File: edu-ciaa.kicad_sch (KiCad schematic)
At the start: 2 parts

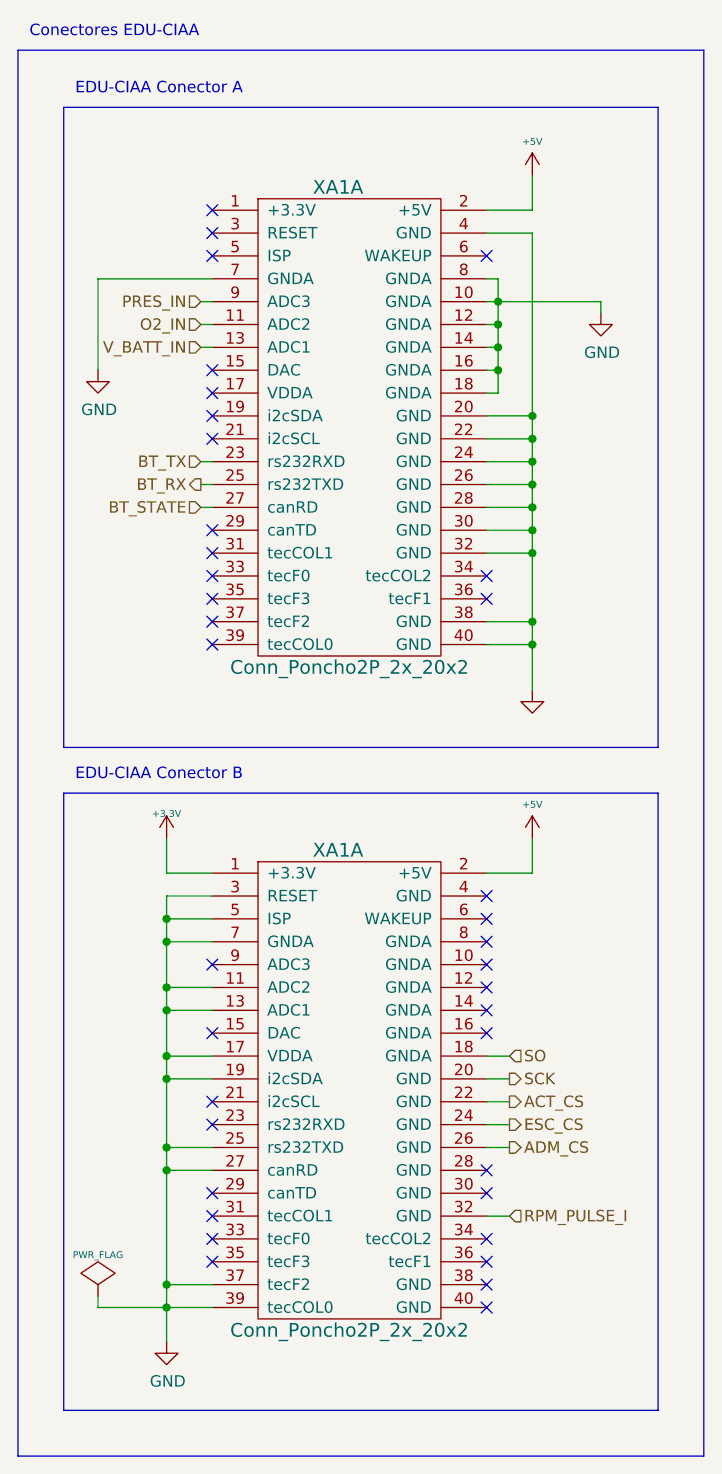
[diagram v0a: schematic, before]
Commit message: Actualizacion a kicad 7, seleccion de ganancia de la etapa de amplificacion de presion de aceite.
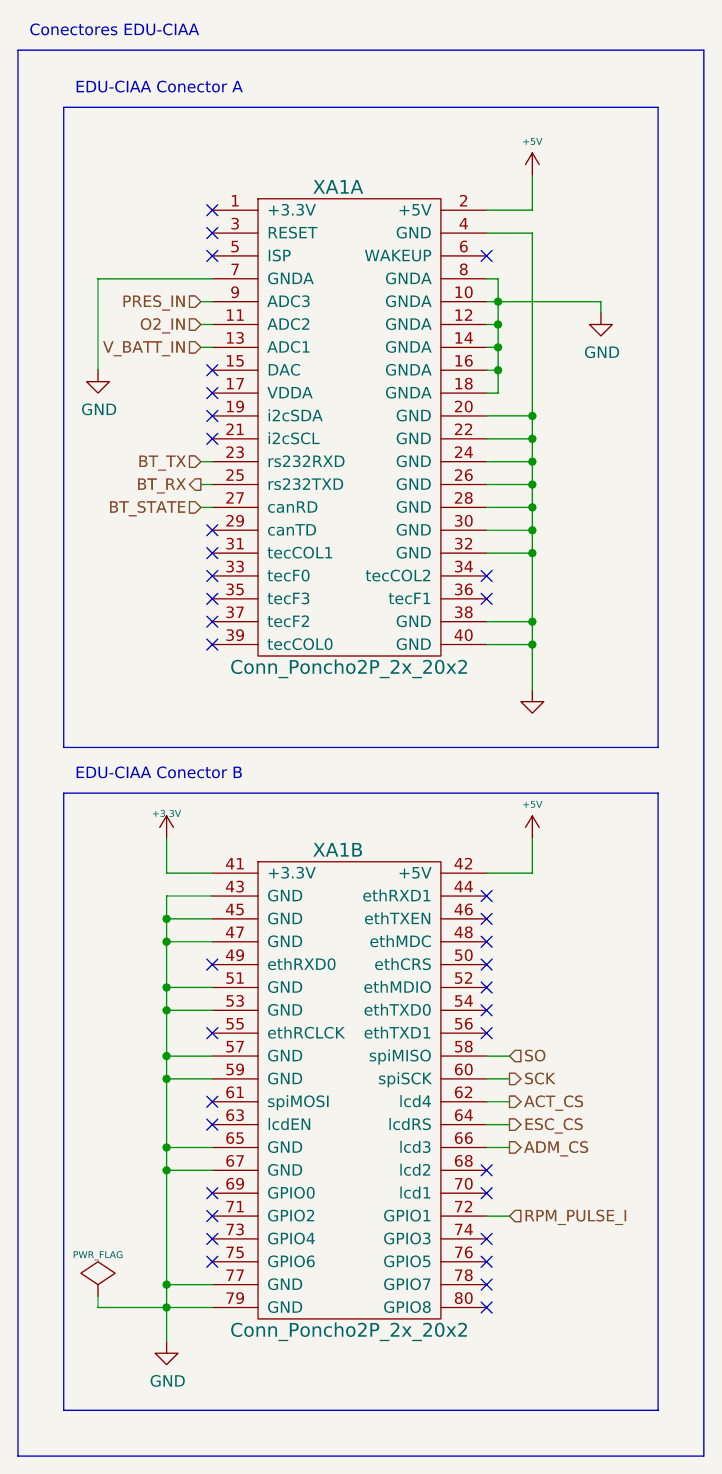
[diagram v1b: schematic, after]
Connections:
- net +3V3: now also XA1.41 (+3.3V); no longer XA1.1 (+3.3V)
- net +5V: now also XA1.42 (+5V); no longer XA1.2 (+5V)
- net ACT_CS: now also XA1.62 (lcd4); no longer XA1.22 (GND)
- net ADM_CS: now also XA1.66 (lcd3); no longer XA1.26 (GND)
- net ESC_CS: now also XA1.64 (lcdRS); no longer XA1.24 (GND)
- net GND: now also XA1.43 (GND), XA1.45 (GND), XA1.47 (GND), XA1.51 (GND), XA1.53 (GND), XA1.57 (GND), XA1.59 (GND), XA1.65 (GND), XA1.67 (GND), XA1.77 (GND), XA1.79 (GND); no longer XA1.11 (ADC2), XA1.13 (ADC1), XA1.17 (VDDA), XA1.19 (i2cSDA), XA1.25 (rs232TXD), XA1.27 (canRD), XA1.3 (RESET), XA1.37 (tecF2), XA1.39 (tecCOL0), XA1.5 (ISP), XA1.7 (GNDA)
- net RPM_PULSE_I: now also XA1.72 (GPIO1); no longer XA1.32 (GND)
- net SCK: now also XA1.60 (spiSCK); no longer XA1.20 (GND)
- net SO: now also XA1.58 (spiMISO); no longer XA1.18 (GNDA)
